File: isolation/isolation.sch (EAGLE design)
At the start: 2 parts

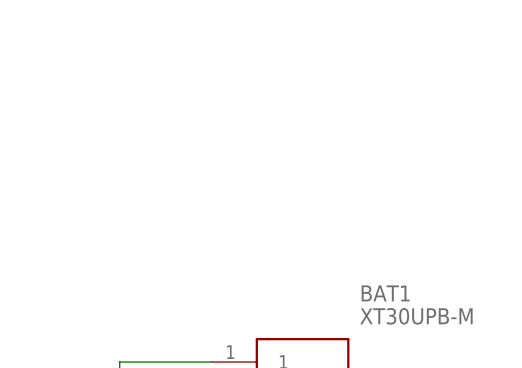
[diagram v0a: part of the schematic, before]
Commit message: power indicator LED
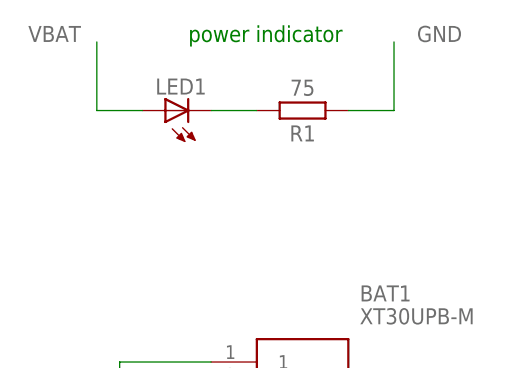
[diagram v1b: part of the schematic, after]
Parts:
- added LED1: (no value), adafruit:LEDCHIPLED_0805
- added R1: 75, Resistor:R_CHIP-0603(1608-METRIC)
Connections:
- new net N$1: LED1.C, R1.2
- net GND: now also R1.1
- net VBAT: now also LED1.A
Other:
- note added: "power indicator"

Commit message: 12v boost schematic complete
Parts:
- added C1, C2: 10u, 52101-101-REV-A_v16:RC-MASTER-SMD_C_0603MP
- added C3: 1u, 52101-101-REV-A_v16:RC-MASTER-SMD_C_0603MP
- added C4, C5, C6, C7: 22u, 52101-101-REV-A_v16:RC-MASTER-SMD_C_0603MP
- added D1: SSA34-E3_5AT, SamacSys_Parts:SSA34-E3_5AT
- added IC1: XTLV61048DBVR, SamacSys_Parts:XTLV61048DBVR
- added L1: 10, BeagleBone_Blue_R3:INDUCTOR
- added R2: 1M, Resistor:R_CHIP-0603(1608-METRIC)
- added R3: 68k, Resistor:R_CHIP-0603(1608-METRIC)
- R1: value 75 -> 47
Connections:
- new net N$2: C3.1, D1.A, IC1.SW, L1.1
- new net N$3: IC1.FB, R2.2, R3.1
- new net VDEP: C2.2, D1.K, R2.1
- net GND: now also C1.2, C2.1, C3.2, C4.1, C5.1, C6.1, C7.1, IC1.GND, R3.2
- net VBAT: now also C1.1, C4.2, C5.2, C6.2, C7.2, IC1.EN, IC1.FREQ, IC1.VIN, L1.2
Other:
- moved on the sheet: LED1, R1

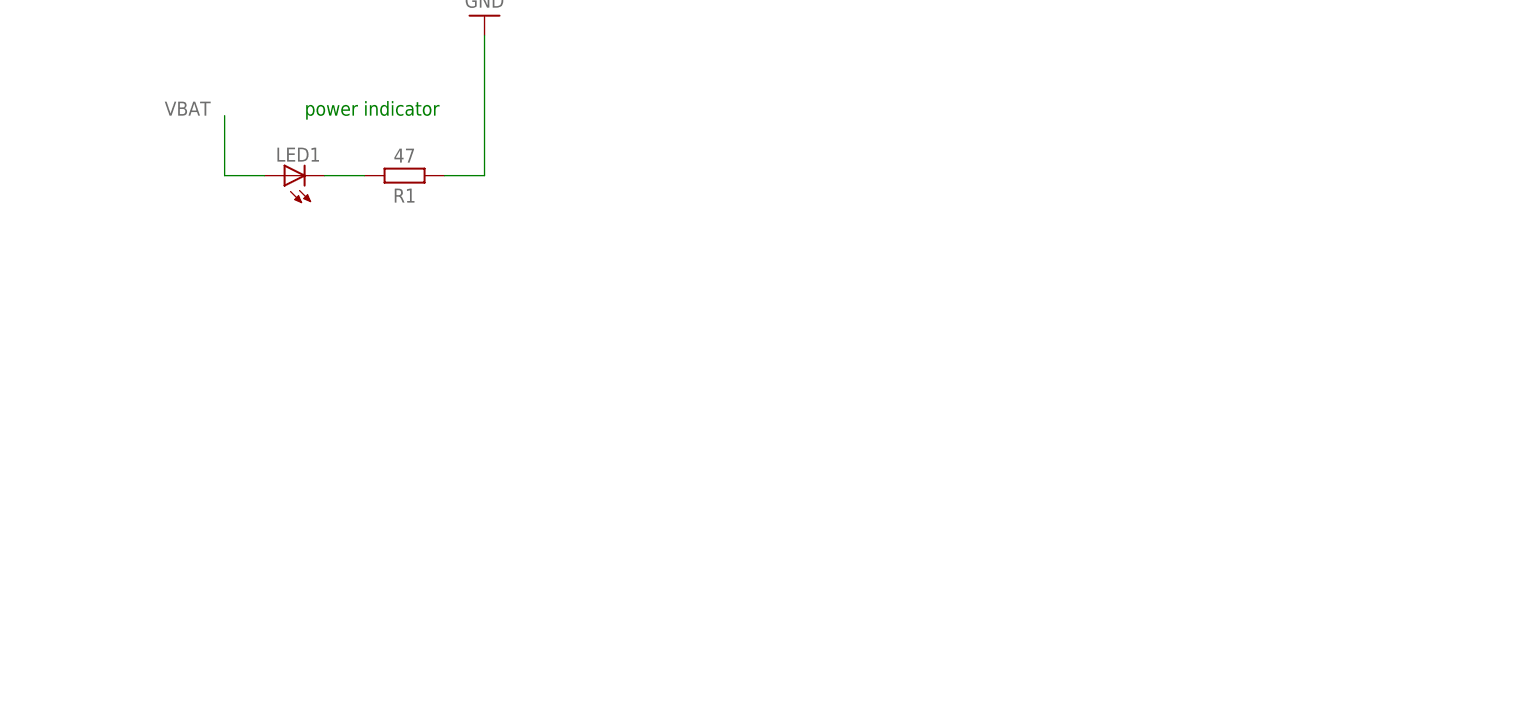
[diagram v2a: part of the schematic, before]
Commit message: headphone jacks for user input
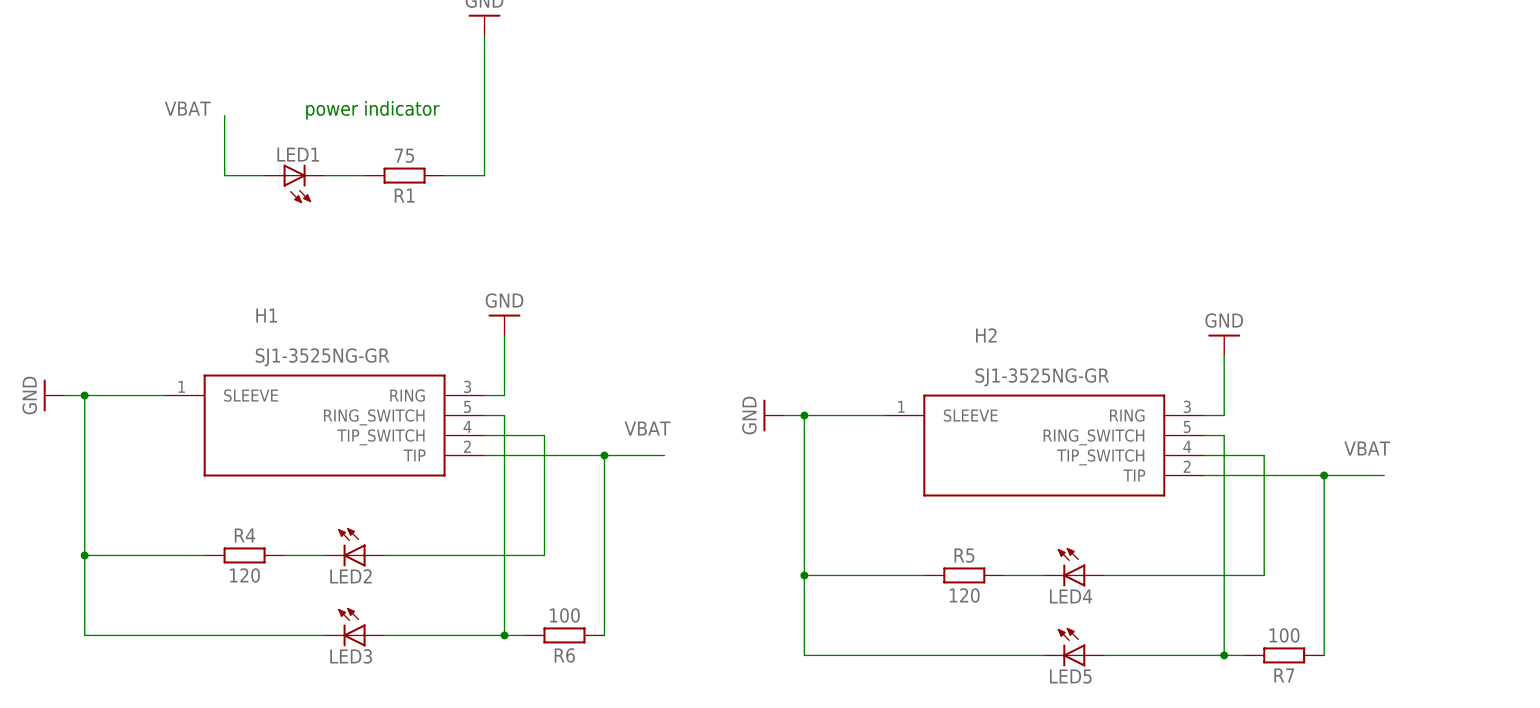
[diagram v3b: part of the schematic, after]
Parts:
- added H1, H2: SJ1-3525NG-GR, SamacSys_Parts:SJ1-3525NG-GR
- added LED2, LED3, LED4, LED5: (no value), adafruit:LEDCHIPLED_0805
- added R4, R5: 120, Resistor:R_CHIP-0603(1608-METRIC)
- added R6, R7: 100, Resistor:R_CHIP-0603(1608-METRIC)
- R1: value 47 -> 75
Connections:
- new net EN1: H1.TIP_SWITCH, LED2.A
- new net EN2: H2.TIP_SWITCH, LED4.A
- new net N$4: H1.RING_SWITCH, LED3.A, R6.2
- new net N$5: LED2.C, R4.2
- new net N$6: LED4.C, R5.2
- new net N$7: H2.RING_SWITCH, LED5.A, R7.2
- net GND: now also H1.RING, H1.SLEEVE, H2.RING, H2.SLEEVE, LED3.C, LED5.C, R4.1, R5.1
- net VBAT: now also H1.TIP, H2.TIP, R6.1, R7.1

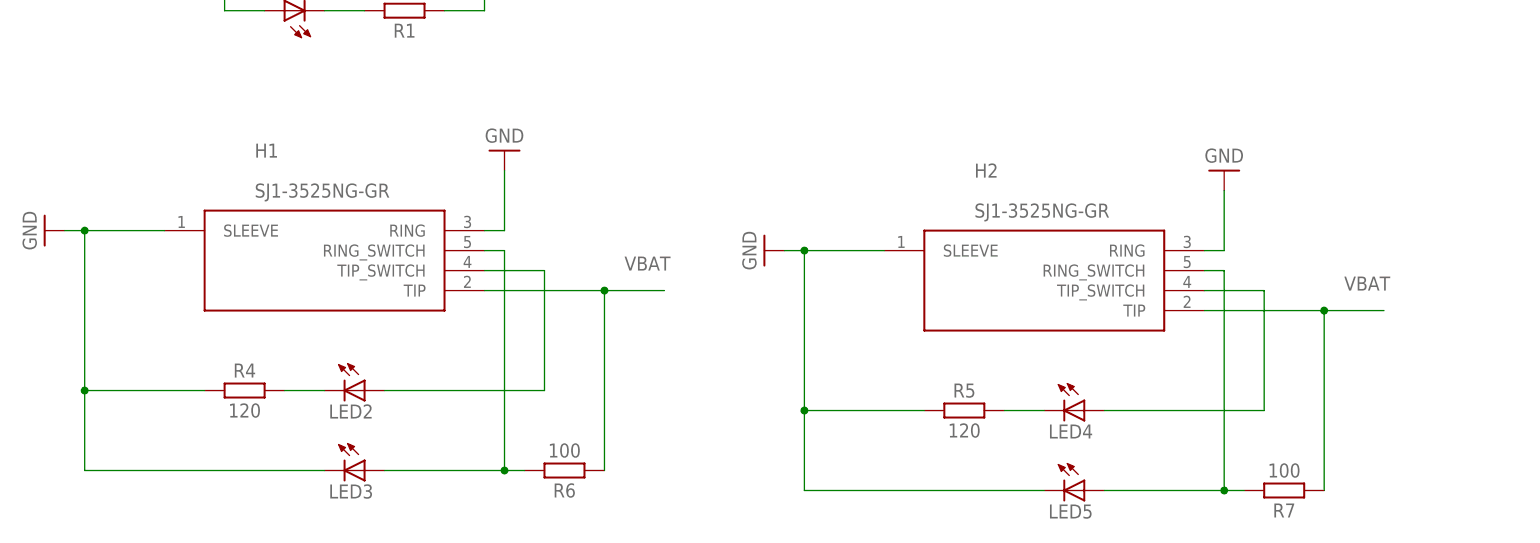
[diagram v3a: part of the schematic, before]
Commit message: fix footprint for caps
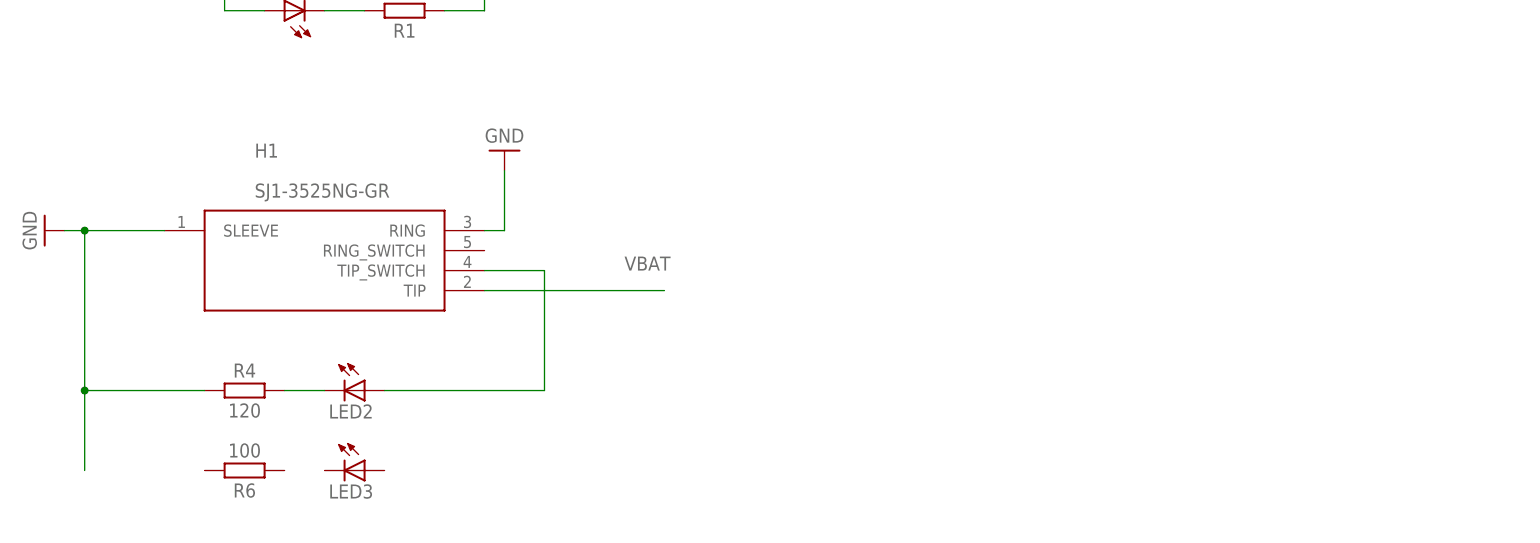
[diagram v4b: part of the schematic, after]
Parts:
- removed H2: SJ1-3525NG-GR, SamacSys_Parts:SJ1-3525NG-GR
- removed LED4, LED5: (no value), adafruit:LEDCHIPLED_0805
- removed R5: 120, Resistor:R_CHIP-0603(1608-METRIC)
- removed R7: 100, Resistor:R_CHIP-0603(1608-METRIC)
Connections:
- removed net EN2: H2.TIP_SWITCH, LED4.A
- removed net N$4: H1.RING_SWITCH, LED3.A, R6.2
- removed net N$6: LED4.C, R5.2
- removed net N$7: H2.RING_SWITCH, LED5.A, R7.2
- net GND: no longer H2.RING, H2.SLEEVE, LED3.C, LED5.C, R5.1
- net VBAT: no longer H2.TIP, R6.1, R7.1
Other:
- moved on the sheet: R6
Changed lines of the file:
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@@
 <part name="R6" library="Resistor" library_urn="urn:adsk.eagle:library:16378527" deviceset="R" device="CHIP-0603(1608-METRIC)" package3d_urn="urn:adsk.eagle:package:16378565/5" technology="_" value="100"/>
 <part name="LED3" library="adafruit" library_urn="urn:adsk.eagle:library:420" deviceset="LED" device="CHIPLED_0805" package3d_urn="urn:adsk.eagle:package:6240559/1"/>
-<part name="SUPPLY9" library="Power_Symbols" library_urn="urn:adsk.eagle:library:16502351" deviceset="GND-BAR" device="" value="GND"/>
-<part name="LED4" library="adafruit" library_urn="urn:adsk.eagle:library:420" deviceset="LED" device="CHIPLED_0805" package3d_urn="urn:adsk.eagle:package:6240559/1"/>
-<part name="R5" library="Resistor" library_urn="urn:adsk.eagle:library:16378527" deviceset="R" device="CHIP-0603(1608-METRIC)" package3d_urn="urn:adsk.eagle:package:16378565/5" technology="_" value="120"/>
-<part name="H2" library="SamacSys_Parts" deviceset="SJ1-3525NG-GR" device=""/>
-<part name="SUPPLY10" library="Power_Symbols" library_urn="urn:adsk.eagle:library:16502351" deviceset="GND-BAR" device="" value="GND"/>
-<part name="R7" library="Resistor" library_urn="urn:adsk.eagle:library:16378527" deviceset="R" device="CHIP-0603(1608-METRIC)" package3d_urn="urn:adsk.eagle:package:16378565/5" technology="_" value="100"/>
-<part name="LED5" library="adafruit" library_urn="urn:adsk.eagle:library:420" deviceset="LED" device="CHIPLED_0805" package3d_urn="urn:adsk.eagle:package:6240559/1"/>
 </parts>
 <sheets>
@@
 <attribute name="VALUE" x="45.72" y="-18.415" size="1.778" layer="96" rot="R180" align="center"/>
 </instance>
-<instance part="R6" gate="G$1" x="53.34" y="-60.96" smashed="yes" rot="R180">
-<attribute name="NAME" x="53.34" y="-63.5" size="1.778" layer="95" rot="R180" align="center"/>
-<attribute name="VALUE" x="53.34" y="-58.42" size="1.778" layer="96" rot="R180" align="center"/>
+<instance part="R6" gate="G$1" x="12.7" y="-60.96" smashed="yes" rot="R180">
+<attribute name="NAME" x="12.7" y="-63.5" size="1.778" layer="95" rot="R180" align="center"/>
+<attribute name="VALUE" x="12.7" y="-58.42" size="1.778" layer="96" rot="R180" align="center"/>
 </instance>
 <instance part="LED3" gate="G$1" x="27.94" y="-60.96" smashed="yes" rot="R270">
 <attribute name="NAME" x="23.368" y="-64.516" size="1.778" layer="95"/>
 <attribute name="VALUE" x="23.368" y="-66.675" size="1.778" layer="96"/>
-</instance>
-<instance part="SUPPLY9" gate="G$1" x="78.74" y="-33.02" smashed="yes" rot="R270">
-<attribute name="VALUE" x="76.835" y="-33.02" size="1.778" layer="96" rot="R270" align="center"/>
-</instance>
-<instance part="LED4" gate="G$1" x="119.38" y="-53.34" smashed="yes" rot="R270">
-<attribute name="NAME" x="114.808" y="-56.896" size="1.778" layer="95"/>
-<attribute name="VALUE" x="114.808" y="-59.055" size="1.778" layer="96"/>
-</instance>
-<instance part="R5" gate="G$1" x="104.14" y="-53.34" smashed="yes">
-<attribute name="NAME" x="104.14" y="-50.8" size="1.778" layer="95" align="center"/>
-<attribute name="VALUE" x="104.14" y="-55.88" size="1.778" layer="96" align="center"/>
-</instance>
-<instance part="H2" gate="G$1" x="93.98" y="-33.02" smashed="yes">
-<attribute name="NAME" x="105.41" y="-22.86" size="1.778" layer="95" align="center-left"/>
-<attribute name="VALUE" x="105.41" y="-27.94" size="1.778" layer="96" align="center-left"/>
-</instance>
-<instance part="SUPPLY10" gate="G$1" x="137.16" y="-22.86" smashed="yes" rot="R180">
-<attribute name="VALUE" x="137.16" y="-20.955" size="1.778" layer="96" rot="R180" align="center"/>
-</instance>
-<instance part="R7" gate="G$1" x="144.78" y="-63.5" smashed="yes" rot="R180">
-<attribute name="NAME" x="144.78" y="-66.04" size="1.778" layer="95" rot="R180" align="center"/>
-<attribute name="VALUE" x="144.78" y="-60.96" size="1.778" layer="96" rot="R180" align="center"/>
-</instance>
-<instance part="LED5" gate="G$1" x="119.38" y="-63.5" smashed="yes" rot="R270">
-<attribute name="NAME" x="114.808" y="-67.056" size="1.778" layer="95"/>
-<attribute name="VALUE" x="114.808" y="-69.215" size="1.778" layer="96"/>
 </instance>
 </instances>
@@
 <pinref part="R4" gate="G$1" pin="1"/>
 <wire x1="7.62" y1="-50.8" x2="-7.62" y2="-50.8" width="0.1524" layer="91"/>
-<pinref part="LED3" gate="G$1" pin="C"/>
-<wire x1="22.86" y1="-60.96" x2="-7.62" y2="-60.96" width="0.1524" layer="91"/>
 <wire x1="-7.62" y1="-60.96" x2="-7.62" y2="-50.8" width="0.1524" layer="91"/>
 <junction x="-7.62" y="-50.8"/>
@@
 <pinref part="H1" gate="G$1" pin="RING"/>
 <wire x1="45.72" y1="-30.48" x2="43.18" y2="-30.48" width="0.1524" layer="91"/>
-</segment>
-<segment>
-<pinref part="SUPPLY9" gate="G$1" pin="GND"/>
-<wire x1="83.82" y1="-33.02" x2="81.28" y2="-33.02" width="0.1524" layer="91"/>
-<wire x1="83.82" y1="-53.34" x2="83.82" y2="-33.02" width="0.1524" layer="91"/>
-<pinref part="H2" gate="G$1" pin="SLEEVE"/>
-<wire x1="93.98" y1="-33.02" x2="83.82" y2="-33.02" width="0.1524" layer="91"/>
-<junction x="83.82" y="-33.02"/>
-<pinref part="R5" gate="G$1" pin="1"/>
-<wire x1="99.06" y1="-53.34" x2="83.82" y2="-53.34" width="0.1524" layer="91"/>
-<pinref part="LED5" gate="G$1" pin="C"/>
-<wire x1="114.3" y1="-63.5" x2="83.82" y2="-63.5" width="0.1524" layer="91"/>
-<wire x1="83.82" y1="-63.5" x2="83.82" y2="-53.34" width="0.1524" layer="91"/>
-<junction x="83.82" y="-53.34"/>
-</segment>
-<segment>
-<pinref part="SUPPLY10" gate="G$1" pin="GND"/>
-<wire x1="137.16" y1="-25.4" x2="137.16" y2="-33.02" width="0.1524" layer="91"/>
-<pinref part="H2" gate="G$1" pin="RING"/>
-<wire x1="137.16" y1="-33.02" x2="134.62" y2="-33.02" width="0.1524" layer="91"/>
 </segment>
 </net>
@@
 <segment>
 <pinref part="H1" gate="G$1" pin="TIP"/>
-<wire x1="43.18" y1="-38.1" x2="58.42" y2="-38.1" width="0.1524" layer="91"/>
-<pinref part="R6" gate="G$1" pin="1"/>
-<wire x1="58.42" y1="-38.1" x2="66.04" y2="-38.1" width="0.1524" layer="91"/>
-<wire x1="58.42" y1="-60.96" x2="58.42" y2="-38.1" width="0.1524" layer="91"/>
-<junction x="58.42" y="-38.1"/>
+<wire x1="43.18" y1="-38.1" x2="66.04" y2="-38.1" width="0.1524" layer="91"/>
 <label x="60.96" y="-35.56" size="1.778" layer="95"/>
-</segment>
-<segment>
-<pinref part="H2" gate="G$1" pin="TIP"/>
-<wire x1="134.62" y1="-40.64" x2="149.86" y2="-40.64" width="0.1524" layer="91"/>
-<pinref part="R7" gate="G$1" pin="1"/>
-<wire x1="149.86" y1="-40.64" x2="157.48" y2="-40.64" width="0.1524" layer="91"/>
-<wire x1="149.86" y1="-63.5" x2="149.86" y2="-40.64" width="0.1524" layer="91"/>
-<junction x="149.86" y="-40.64"/>
-<label x="152.4" y="-38.1" size="1.778" layer="95"/>
 </segment>
 </net>
@@
 </segment>
 </net>
-<net name="N$4" class="0">
-<segment>
-<pinref part="H1" gate="G$1" pin="RING_SWITCH"/>
-<wire x1="43.18" y1="-33.02" x2="45.72" y2="-33.02" width="0.1524" layer="91"/>
-<wire x1="45.72" y1="-33.02" x2="45.72" y2="-60.96" width="0.1524" layer="91"/>
-<pinref part="R6" gate="G$1" pin="2"/>
-<wire x1="45.72" y1="-60.96" x2="48.26" y2="-60.96" width="0.1524" layer="91"/>
-<pinref part="LED3" gate="G$1" pin="A"/>
-<wire x1="30.48" y1="-60.96" x2="45.72" y2="-60.96" width="0.1524" layer="91"/>
-<junction x="45.72" y="-60.96"/>
-</segment>
-</net>
-<net name="EN2" class="0">
-<segment>
-<pinref part="LED4" gate="G$1" pin="A"/>
-<pinref part="H2" gate="G$1" pin="TIP_SWITCH"/>
-<wire x1="134.62" y1="-38.1" x2="142.24" y2="-38.1" width="0.1524" layer="91"/>
-<wire x1="142.24" y1="-38.1" x2="142.24" y2="-53.34" width="0.1524" layer="91"/>
-<wire x1="142.24" y1="-53.34" x2="121.92" y2="-53.34" width="0.1524" layer="91"/>
-</segment>
-</net>
-<net name="N$6" class="0">
-<segment>
-<pinref part="LED4" gate="G$1" pin="C"/>
-<pinref part="R5" gate="G$1" pin="2"/>
-<wire x1="114.3" y1="-53.34" x2="109.22" y2="-53.34" width="0.1524" layer="91"/>
-</segment>
-</net>
-<net name="N$7" class="0">
-<segment>
-<pinref part="H2" gate="G$1" pin="RING_SWITCH"/>
-<wire x1="134.62" y1="-35.56" x2="137.16" y2="-35.56" width="0.1524" layer="91"/>
-<wire x1="137.16" y1="-35.56" x2="137.16" y2="-63.5" width="0.1524" layer="91"/>
-<pinref part="R7" gate="G$1" pin="2"/>
-<wire x1="137.16" y1="-63.5" x2="139.7" y2="-63.5" width="0.1524" layer="91"/>
-<pinref part="LED5" gate="G$1" pin="A"/>
-<wire x1="121.92" y1="-63.5" x2="137.16" y2="-63.5" width="0.1524" layer="91"/>
-<junction x="137.16" y="-63.5"/>
-</segment>
-</net>
